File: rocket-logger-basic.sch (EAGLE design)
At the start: 60 parts, among them IC1 CC430F513X, Q2 MOSFET-PCHANNEL, U2 MAX1555, U3 MCP73831, X1 0896BM15A0001, X2 USB-MICROB, X3 SMA-142-0701-801/806

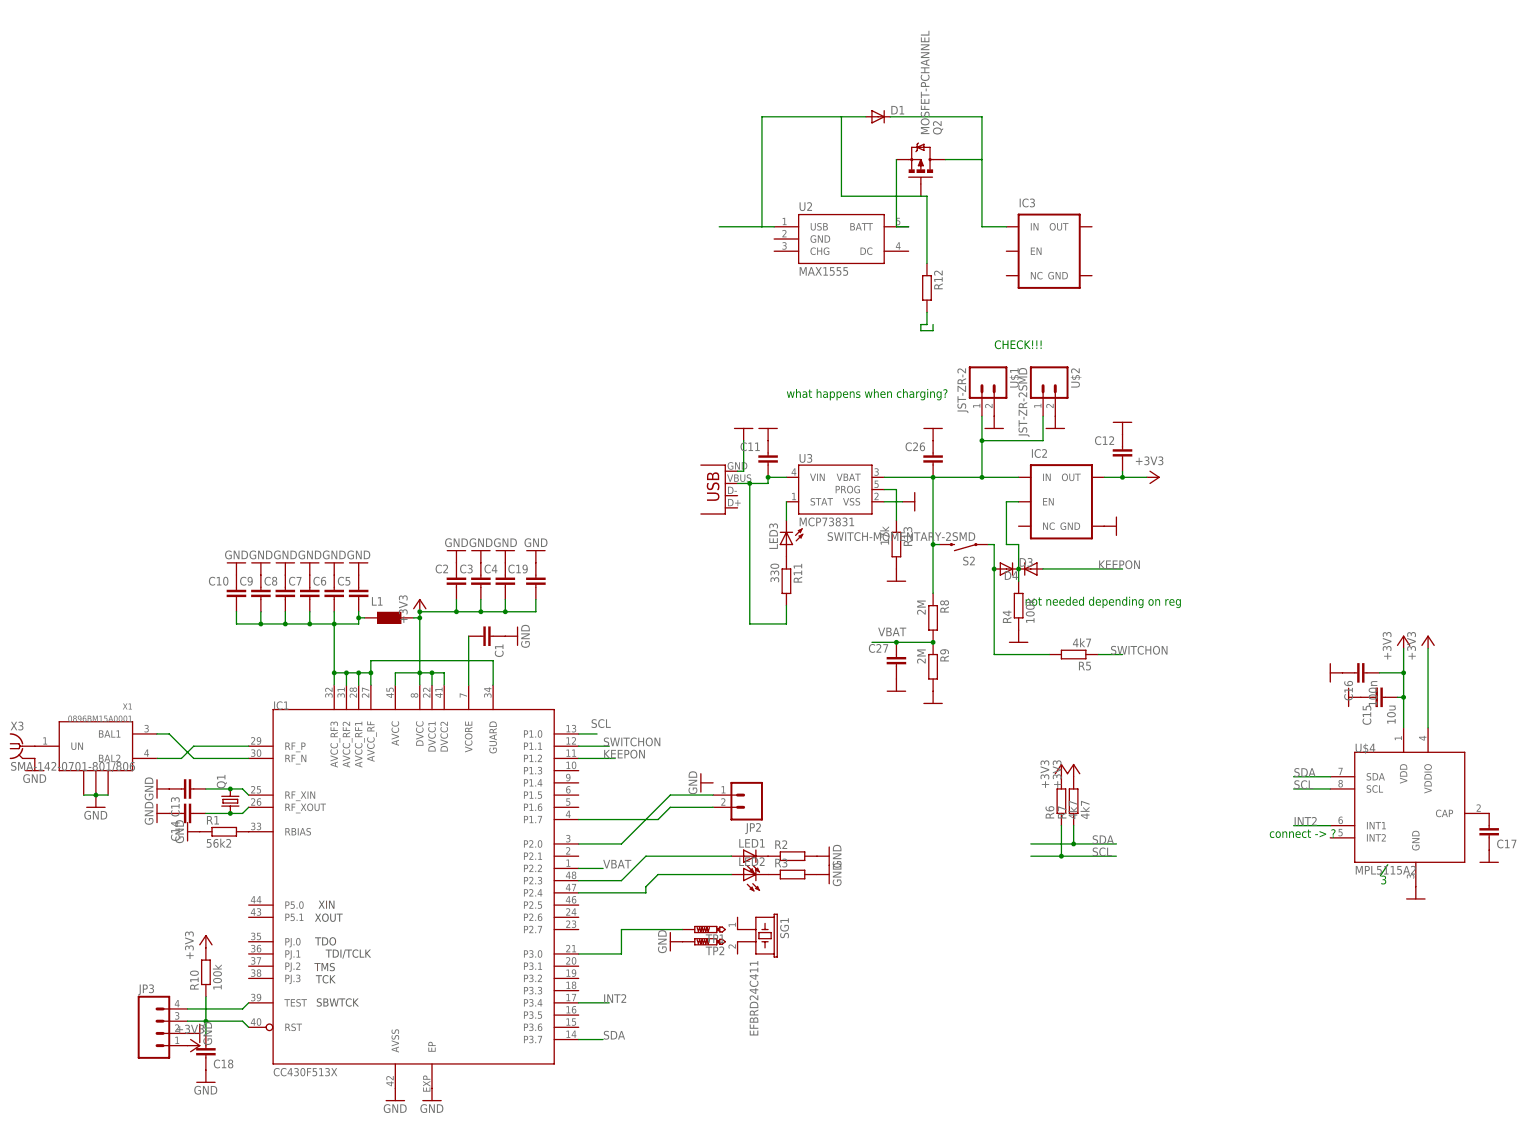
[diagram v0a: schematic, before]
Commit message: updating component values
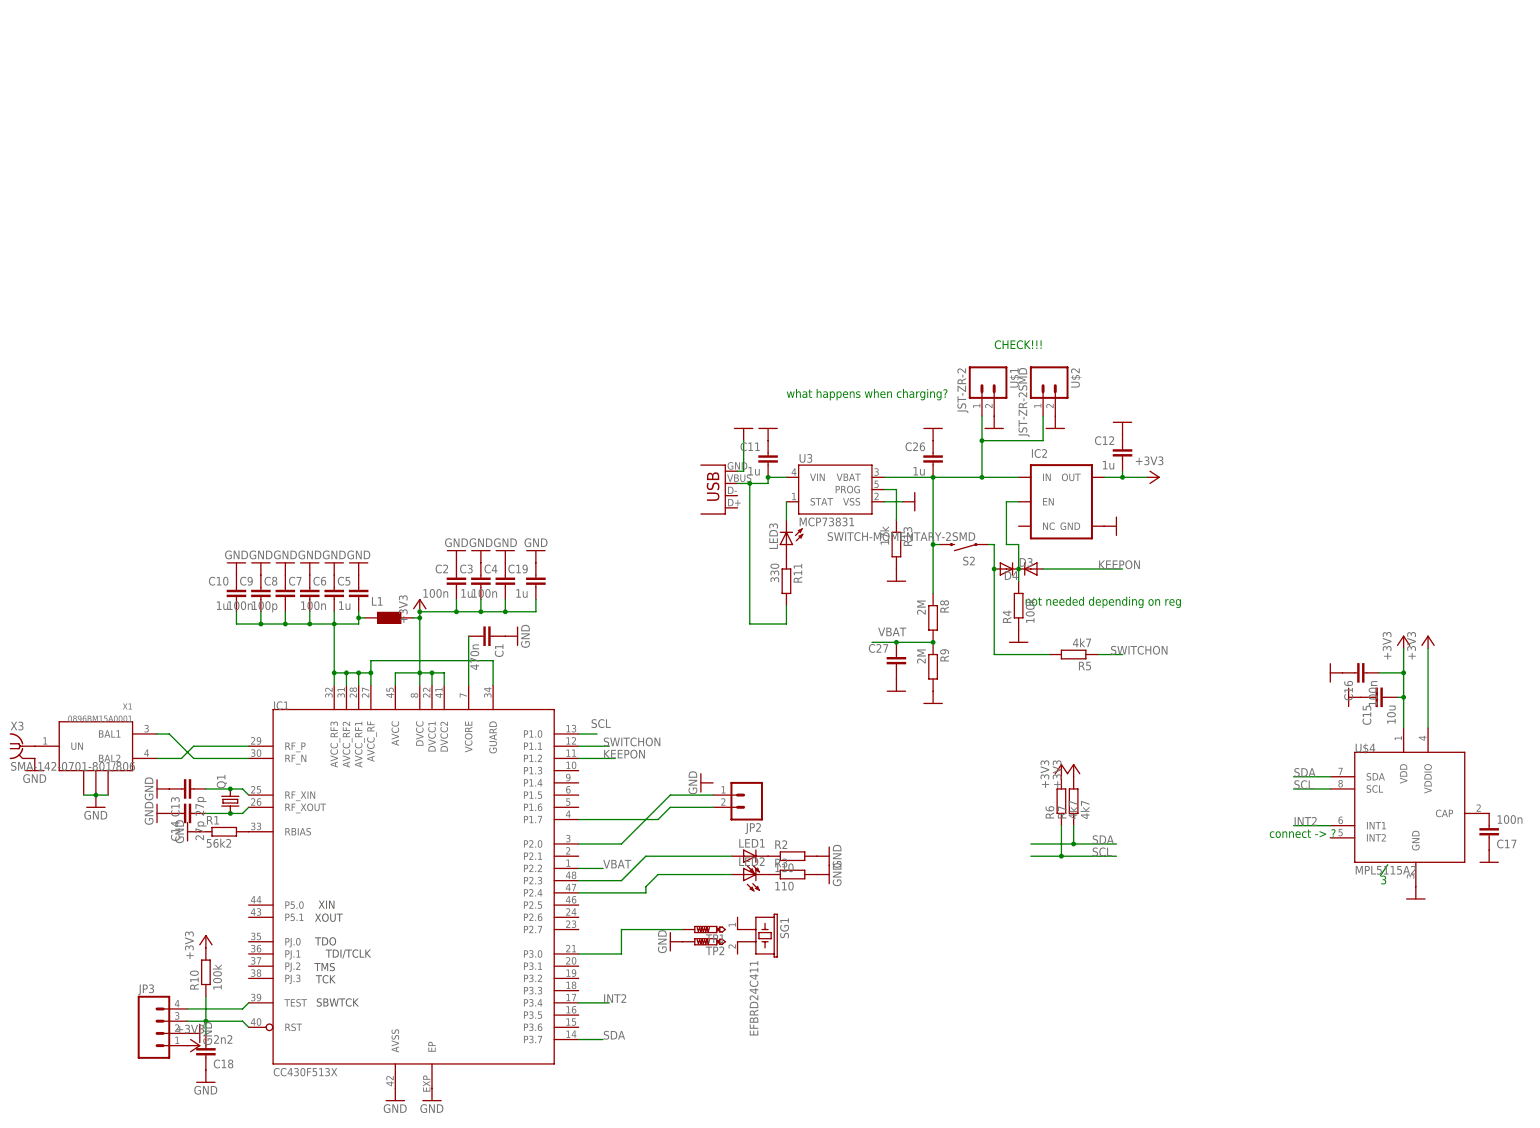
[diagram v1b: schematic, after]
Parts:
- removed D1: (no value), diode:DIODE-SOD523
- removed IC3: (no value), SparkFun:V_REG_TPS76433SOT23-5
- removed Q2: MOSFET-PCHANNEL, SparkFun:MOSFET-PCHANNEL
- removed R12: (no value), rcl:R-EU_R0402
- removed U2: MAX1555, SparkFun:MAX1555
- C1: value (none) -> 470n
- C10, C11, C12, C19, C26, C3, C5: value (none) -> 1u
- C13, C14: value (none) -> 27p
- C17, C2, C4, C6, C9: value (none) -> 100n
- C18: value (none) -> 2n2
- C8: value (none) -> 100p
- R2, R3: value (none) -> 110
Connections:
- removed net N$20: D1.C, IC3.IN, Q2.D
- removed net N$21: D1.A, Q2.G, R12.1, U2.USB
- removed net N$22: R12.2
- removed net N$27: Q2.S, U2.BATT
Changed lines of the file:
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@@
 <part name="LED2" library="SparkFun" deviceset="LED" device="0603"/>
 <part name="IC2" library="SparkFun" deviceset="V_REG_TPS76433" device="SOT23-5"/>
-<part name="C1" library="resistor" deviceset="C-EU" device="C0402"/>
-<part name="C2" library="resistor" deviceset="C-EU" device="C0402"/>
-<part name="C3" library="resistor" deviceset="C-EU" device="C0402"/>
-<part name="C4" library="resistor" deviceset="C-EU" device="C0402"/>
-<part name="C5" library="resistor" deviceset="C-EU" device="C0402"/>
-<part name="C6" library="resistor" deviceset="C-EU" device="C0402"/>
+<part name="C1" library="resistor" deviceset="C-EU" device="C0402" value="470n"/>
+<part name="C2" library="resistor" deviceset="C-EU" device="C0402" value="100n"/>
+<part name="C3" library="resistor" deviceset="C-EU" device="C0402" value="1u"/>
+<part name="C4" library="resistor" deviceset="C-EU" device="C0402" value="100n"/>
+<part name="C5" library="resistor" deviceset="C-EU" device="C0402" value="1u"/>
+<part name="C6" library="resistor" deviceset="C-EU" device="C0402" value="100n"/>
 <part name="C7" library="resistor" deviceset="C-EU" device="C0402"/>
-<part name="C8" library="resistor" deviceset="C-EU" device="C0402"/>
-<part name="C9" library="resistor" deviceset="C-EU" device="C0402"/>
-<part name="C10" library="resistor" deviceset="C-EU" device="C0402"/>
+<part name="C8" library="resistor" deviceset="C-EU" device="C0402" value="100p"/>
+<part name="C9" library="resistor" deviceset="C-EU" device="C0402" value="100n"/>
+<part name="C10" library="resistor" deviceset="C-EU" device="C0402" value="1u"/>
 <part name="GND1" library="supply1" deviceset="GND" device=""/>
 <part name="GND2" library="supply1" deviceset="GND" device=""/>
@@
 <part name="X2" library="SparkFun" deviceset="USB" device="-MICROB"/>
 <part name="GND32" library="SparkFun" deviceset="GND" device=""/>
-<part name="C11" library="resistor" deviceset="C-EU" device="C0402"/>
+<part name="C11" library="resistor" deviceset="C-EU" device="C0402" value="1u"/>
 <part name="GND14" library="SparkFun" deviceset="GND" device=""/>
 <part name="GND16" library="SparkFun" deviceset="GND" device=""/>
 <part name="+3V1" library="supply1" deviceset="+3V3" device=""/>
-<part name="C12" library="resistor" deviceset="C-EU" device="C0402"/>
+<part name="C12" library="resistor" deviceset="C-EU" device="C0402" value="1u"/>
 <part name="GND17" library="SparkFun" deviceset="GND" device=""/>
 <part name="Q1" library="SparkFun" deviceset="CRYSTAL" device="5X3"/>
-<part name="C13" library="resistor" deviceset="C-EU" device="C0402"/>
-<part name="C14" library="resistor" deviceset="C-EU" device="C0402"/>
+<part name="C13" library="resistor" deviceset="C-EU" device="C0402" value="27p"/>
+<part name="C14" library="resistor" deviceset="C-EU" device="C0402" value="27p"/>
 <part name="GND18" library="supply1" deviceset="GND" device=""/>
 <part name="GND19" library="supply1" deviceset="GND" device=""/>
@@
 <part name="X3" library="con-coax" deviceset="SMA-" device="142-0701-801/806"/>
 <part name="GND22" library="supply1" deviceset="GND" device=""/>
-<part name="R2" library="rcl" deviceset="R-EU_" device="R0402"/>
-<part name="R3" library="rcl" deviceset="R-EU_" device="R0402"/>
+<part name="R2" library="rcl" deviceset="R-EU_" device="R0402" value="110"/>
+<part name="R3" library="rcl" deviceset="R-EU_" device="R0402" value="110"/>
 <part name="C15" library="resistor" deviceset="C-EU" device="C0402" value="10u"/>
 <part name="C16" library="resistor" deviceset="C-EU" device="C0402" value="100n"/>
@@
 <part name="GND26" library="SparkFun" deviceset="GND" device=""/>
 <part name="GND27" library="SparkFun" deviceset="GND" device=""/>
-<part name="C17" library="resistor" deviceset="C-EU" device="C0402"/>
+<part name="C17" library="resistor" deviceset="C-EU" device="C0402" value="100n"/>
 <part name="GND28" library="SparkFun" deviceset="GND" device=""/>
 <part name="R4" library="rcl" deviceset="R-EU_" device="R0402" value="100k"/>
@@
 <part name="R5" library="rcl" deviceset="R-EU_" device="R0402" value="4k7"/>
 <part name="SG1" library="buzzer" deviceset="EFB?" device="RD24C411"/>
-<part name="C26" library="resistor" deviceset="C-EU" device="C0402"/>
+<part name="C26" library="resistor" deviceset="C-EU" device="C0402" value="1u"/>
 <part name="GND46" library="SparkFun" deviceset="GND" device=""/>
 <part name="GND23" library="supply1" deviceset="GND" device=""/>
@@
 <part name="GND49" library="SparkFun" deviceset="GND" device=""/>
 <part name="R10" library="rcl" deviceset="R-EU_" device="R0402" value="100k"/>
-<part name="C18" library="resistor" deviceset="C-EU" device="C0402"/>
+<part name="C18" library="resistor" deviceset="C-EU" device="C0402" value="2n2"/>
 <part name="GND29" library="supply1" deviceset="GND" device=""/>
 <part name="+3V2" library="supply1" deviceset="+3V3" device=""/>
@@
 <part name="R11" library="rcl" deviceset="R-EU_" device="R0402" value="330"/>
 <part name="LED3" library="SparkFun" deviceset="LED" device="0603"/>
-<part name="U2" library="SparkFun" deviceset="MAX1555" device=""/>
-<part name="IC3" library="SparkFun" deviceset="V_REG_TPS76433" device="SOT23-5"/>
-<part name="D1" library="diode" deviceset="DIODE-" device="SOD523"/>
-<part name="Q2" library="SparkFun" deviceset="MOSFET-PCHANNEL" device=""/>
-<part name="R12" library="rcl" deviceset="R-EU_" device="R0402"/>
 <part name="U$1" library="Mine" deviceset="JST-ZR-2" device=""/>
 <part name="U$2" library="Mine" deviceset="JST-ZR-2" device="SMD"/>
@@
 <part name="GND34" library="SparkFun" deviceset="GND" device=""/>
 <part name="GND35" library="SparkFun" deviceset="GND" device=""/>
-<part name="C19" library="resistor" deviceset="C-EU" device="C0402"/>
+<part name="C19" library="resistor" deviceset="C-EU" device="C0402" value="1u"/>
 <part name="GND13" library="supply1" deviceset="GND" device=""/>
 </parts>
@@
 <instance part="R11" gate="G$1" x="109.22" y="207.01" rot="R270"/>
 <instance part="LED3" gate="G$1" x="109.22" y="214.63" rot="R180"/>
-<instance part="U2" gate="G$1" x="121.92" y="278.13"/>
-<instance part="IC3" gate="G$1" x="162.56" y="273.05"/>
-<instance part="D1" gate="G$1" x="128.27" y="303.53"/>
-<instance part="Q2" gate="G$1" x="137.16" y="294.64" rot="MR90"/>
-<instance part="R12" gate="G$1" x="138.43" y="267.97" rot="R270"/>
 <instance part="U$1" gate="G$1" x="149.86" y="248.92" rot="R270"/>
 <instance part="U$2" gate="G$1" x="162.56" y="248.92" rot="R270"/>
@@
 </segment>
 </net>
-<net name="N$20" class="0">
-<segment>
-<pinref part="D1" gate="G$1" pin="C"/>
-<wire x1="130.81" y1="303.53" x2="149.86" y2="303.53" width="0.1524" layer="91"/>
-<wire x1="149.86" y1="303.53" x2="149.86" y2="294.64" width="0.1524" layer="91"/>
-<pinref part="IC3" gate="G$1" pin="IN"/>
-<wire x1="149.86" y1="294.64" x2="149.86" y2="280.67" width="0.1524" layer="91"/>
-<wire x1="149.86" y1="280.67" x2="154.94" y2="280.67" width="0.1524" layer="91"/>
-<pinref part="Q2" gate="G$1" pin="D"/>
-<wire x1="142.24" y1="294.64" x2="149.86" y2="294.64" width="0.1524" layer="91"/>
-</segment>
-</net>
-<net name="N$21" class="0">
-<segment>
-<pinref part="Q2" gate="G$1" pin="G"/>
-<wire x1="137.16" y1="287.02" x2="138.43" y2="287.02" width="0.1524" layer="91"/>
-<wire x1="138.43" y1="287.02" x2="138.43" y2="273.05" width="0.1524" layer="91"/>
-<pinref part="R12" gate="G$1" pin="1"/>
-<pinref part="U2" gate="G$1" pin="USB"/>
-<wire x1="106.68" y1="280.67" x2="104.14" y2="280.67" width="0.1524" layer="91"/>
-<wire x1="104.14" y1="280.67" x2="95.25" y2="280.67" width="0.1524" layer="91"/>
-<wire x1="104.14" y1="280.67" x2="104.14" y2="303.53" width="0.1524" layer="91"/>
-<pinref part="D1" gate="G$1" pin="A"/>
-<wire x1="104.14" y1="303.53" x2="120.65" y2="303.53" width="0.1524" layer="91"/>
-<wire x1="120.65" y1="303.53" x2="125.73" y2="303.53" width="0.1524" layer="91"/>
-<wire x1="137.16" y1="287.02" x2="120.65" y2="287.02" width="0.1524" layer="91"/>
-<wire x1="120.65" y1="287.02" x2="120.65" y2="303.53" width="0.1524" layer="91"/>
-</segment>
-</net>
-<net name="N$22" class="0">
-<segment>
-<pinref part="R12" gate="G$1" pin="2"/>
-<wire x1="138.43" y1="262.89" x2="138.43" y2="260.35" width="0.1524" layer="91"/>
-<wire x1="138.43" y1="260.35" x2="137.16" y2="260.35" width="0.1524" layer="91"/>
-<wire x1="137.16" y1="260.35" x2="137.16" y2="259.08" width="0.1524" layer="91"/>
-<wire x1="137.16" y1="259.08" x2="139.7" y2="259.08" width="0.1524" layer="91"/>
-<wire x1="139.7" y1="259.08" x2="139.7" y2="260.35" width="0.1524" layer="91"/>
-</segment>
-</net>
-<net name="N$27" class="0">
-<segment>
-<pinref part="U2" gate="G$1" pin="BATT"/>
-<pinref part="Q2" gate="G$1" pin="S"/>
-<wire x1="134.62" y1="280.67" x2="132.08" y2="280.67" width="0.1524" layer="91"/>
-<wire x1="132.08" y1="280.67" x2="132.08" y2="294.64" width="0.1524" layer="91"/>
-</segment>
-</net>

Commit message: changing value
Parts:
- C26: value 1u -> 4u7
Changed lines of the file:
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@@
 <part name="R5" library="rcl" deviceset="R-EU_" device="R0402" value="4k7"/>
 <part name="SG1" library="buzzer" deviceset="EFB?" device="RD24C411"/>
-<part name="C26" library="resistor" deviceset="C-EU" device="C0402" value="1u"/>
+<part name="C26" library="resistor" deviceset="C-EU" device="C0402" value="4u7"/>
 <part name="GND46" library="SparkFun" deviceset="GND" device=""/>
 <part name="GND23" library="supply1" deviceset="GND" device=""/>
